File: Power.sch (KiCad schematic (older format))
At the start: 21 parts, among them CN2 XT30PW, Q1 TPN1R603PL, Q2 TPN1R603PL, Q3 TPN1R603PL, Q4 TPN1R603PL, U1 DGD0506A, U3 DGD0506A, U7 MCP6C02T

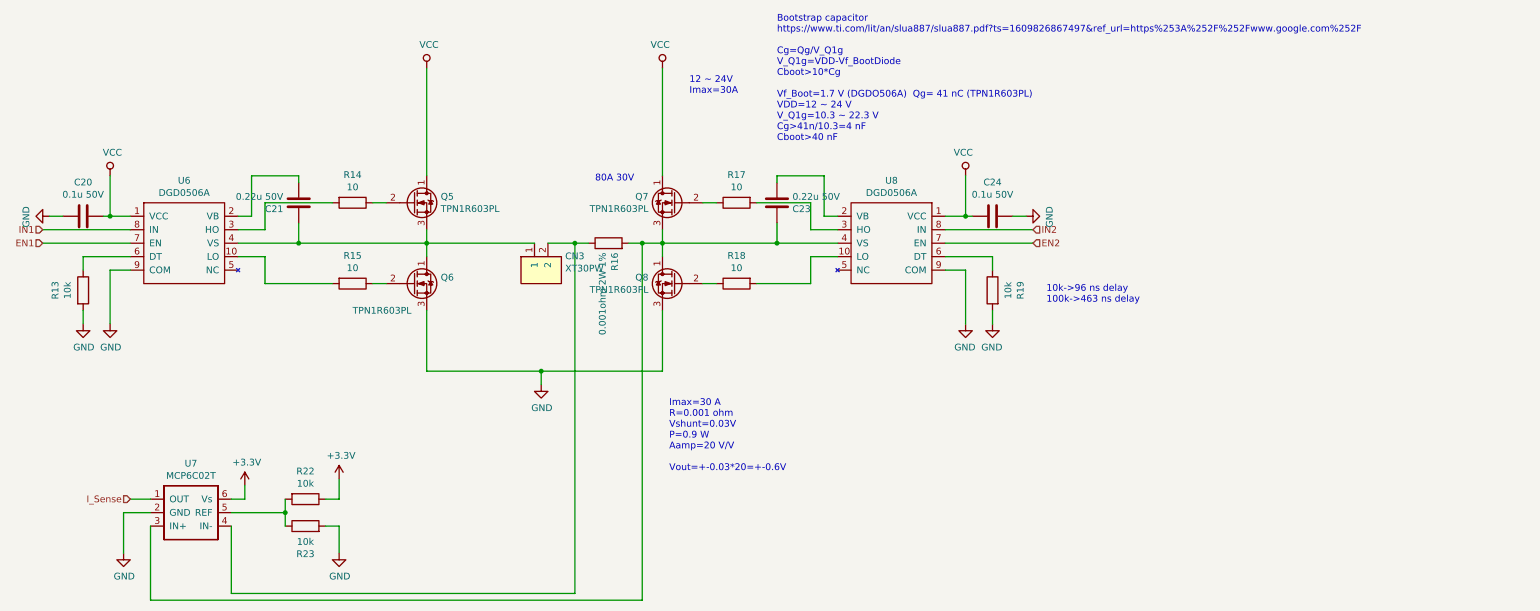
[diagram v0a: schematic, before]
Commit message: add debug pin and fix AVDD
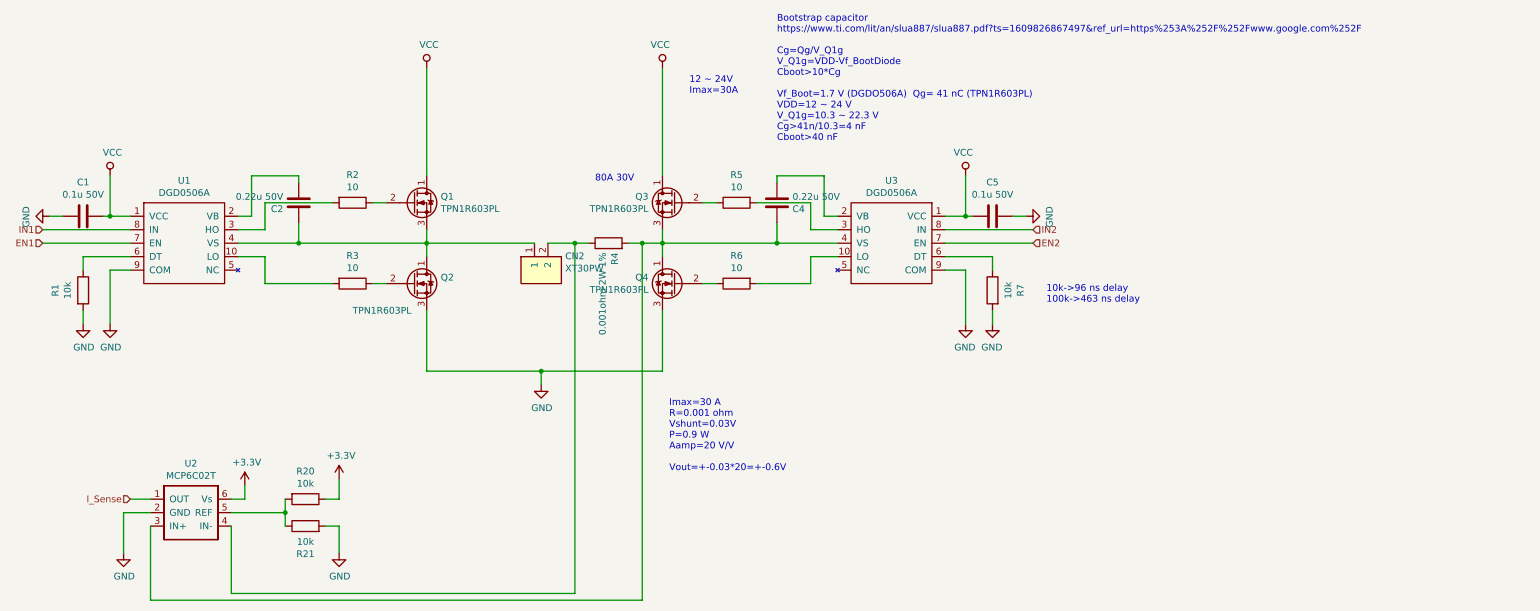
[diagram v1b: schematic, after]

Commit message: v1.1
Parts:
- added C27: 0.1u 50V, Capacitor_SMD:C_0402_1005Metric, symbol Device:C
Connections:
- net +3V3: now also C27.2
- net GND: now also C27.1
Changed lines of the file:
@@
 	3450 5600 3550 5600
-Wire Wire Line
-	3550 5600 3550 5500
 Wire Wire Line
 	5750 4750 5750 4650
@@
 Wire Wire Line
 	5800 3700 6000 3700
+$Comp
+L Device:C C?
+U 1 1 62B995F9
+P 3650 5700
+AR Path="/6260775B/62B995F9" Ref="C?"  Part="1"
+AR Path="/625A1E06/62B995F9" Ref="C27"  Part="1"
+AR Path="/62781A5B/62B995F9" Ref="C28"  Part="1"
+F 0 "C27" V 3398 5700 50  0000 C CNN
+F 1 "0.1u 50V" V 3489 5700 50  0000 C CNN
+F 2 "Capacitor_SMD:C_0402_1005Metric" H 3688 5550 50  0001 C CNN
+F 3 "~" H 3650 5700 50  0001 C CNN
+	1    3650 5700
+	-1   0    0    1
+$EndComp
+Wire Wire Line
+	3550 5500 3550 5550
+Wire Wire Line
+	3650 5550 3550 5550
+Connection ~ 3550 5550
+Wire Wire Line
+	3550 5550 3550 5600
+$Comp
+L power:GND #PWR041
+U 1 1 62B9F70E
+P 3650 6000
+AR Path="/625A1E06/62B9F70E" Ref="#PWR041"  Part="1"
+AR Path="/625A1EDE/62B9F70E" Ref="#PWR?"  Part="1"
+AR Path="/6260775B/62B9F70E" Ref="#PWR?"  Part="1"
+AR Path="/62781A5B/62B9F70E" Ref="#PWR045"  Part="1"
+F 0 "#PWR041" H 3650 5750 50  0001 C CNN
+F 1 "GND" H 3655 5827 50  0000 C CNN
+F 2 "" H 3650 6000 50  0001 C CNN
+F 3 "" H 3650 6000 50  0001 C CNN
+	1    3650 6000
+	1    0    0    -1
+$EndComp
+Wire Wire Line
+	3650 6000 3650 5850
 $EndSCHEMATC

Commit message: kicad5
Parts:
- CN2: symbol maki_lib:XT30PW -> RP_MD-rescue:XT30PW-maki_lib
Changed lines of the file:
@@
 	4250 5800 4250 6000
 $Comp
-L maki_lib:XT30PW CN2
+L RP_MD-rescue:XT30PW-maki_lib CN2
 U 1 1 627A7B14
 P 5700 3800
